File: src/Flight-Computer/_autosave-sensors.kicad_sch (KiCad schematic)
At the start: 36 parts, among them P5 440054-3, P6 440054-3, P7 440054-3, P9 440054-3, Q3 QS5U17TR, Q4 QS5U17TR, Q5 QS5U17TR, Q6 QS5U17TR, U11 BMP390, U8 MPU-9250, U9 MAX-8C-0-10

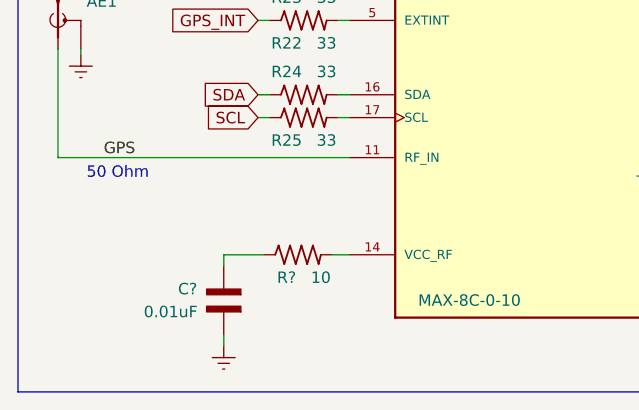
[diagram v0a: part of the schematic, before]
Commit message: added inductor to lib files
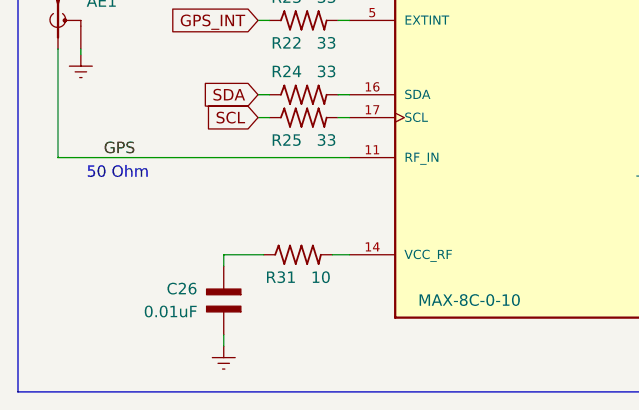
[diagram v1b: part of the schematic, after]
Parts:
- gave numbers to parts that had none: 2
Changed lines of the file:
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@@
   (symbol (lib_id "Flight-Computer:Earth") (at 41.275 142.24 0) (unit 1)
     (in_bom yes) (on_board yes) (fields_autoplaced)
-    (property "Reference" "#PWR?" (id 0) (at 41.275 148.59 0)
+    (property "Reference" "#PWR057" (id 0) (at 41.275 148.59 0)
       (effects (font (size 1.27 1.27)) hide)
     )
@@
   (symbol (lib_id "Flight-Computer:RES_0603") (at 49.53 132.08 0) (unit 1)
     (in_bom yes) (on_board yes)
-    (property "Reference" "R?" (id 0) (at 48.26 134.62 0))
+    (property "Reference" "R31" (id 0) (at 47.625 134.62 0))
     (property "Value" "10" (id 1) (at 52.07 134.62 0))
     (property "Footprint" "" (id 2) (at 50.8 144.78 0)
@@
   (symbol (lib_id "Flight-Computer:CAP_0603") (at 41.275 137.16 90) (unit 1)
     (in_bom yes) (on_board yes)
-    (property "Reference" "C?" (id 0) (at 36.195 135.89 90)
-      (effects (font (size 1.27 1.27)) (justify right))
-    )
+    (property "Reference" "C26" (id 0) (at 34.925 135.89 90)
+      (effects (font (size 1.27 1.27)) (justify right))
+    )
